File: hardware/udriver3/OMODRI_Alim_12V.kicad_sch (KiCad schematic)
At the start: 21 parts, among them U15 MP4572GQB, U9 TPSM560R6H

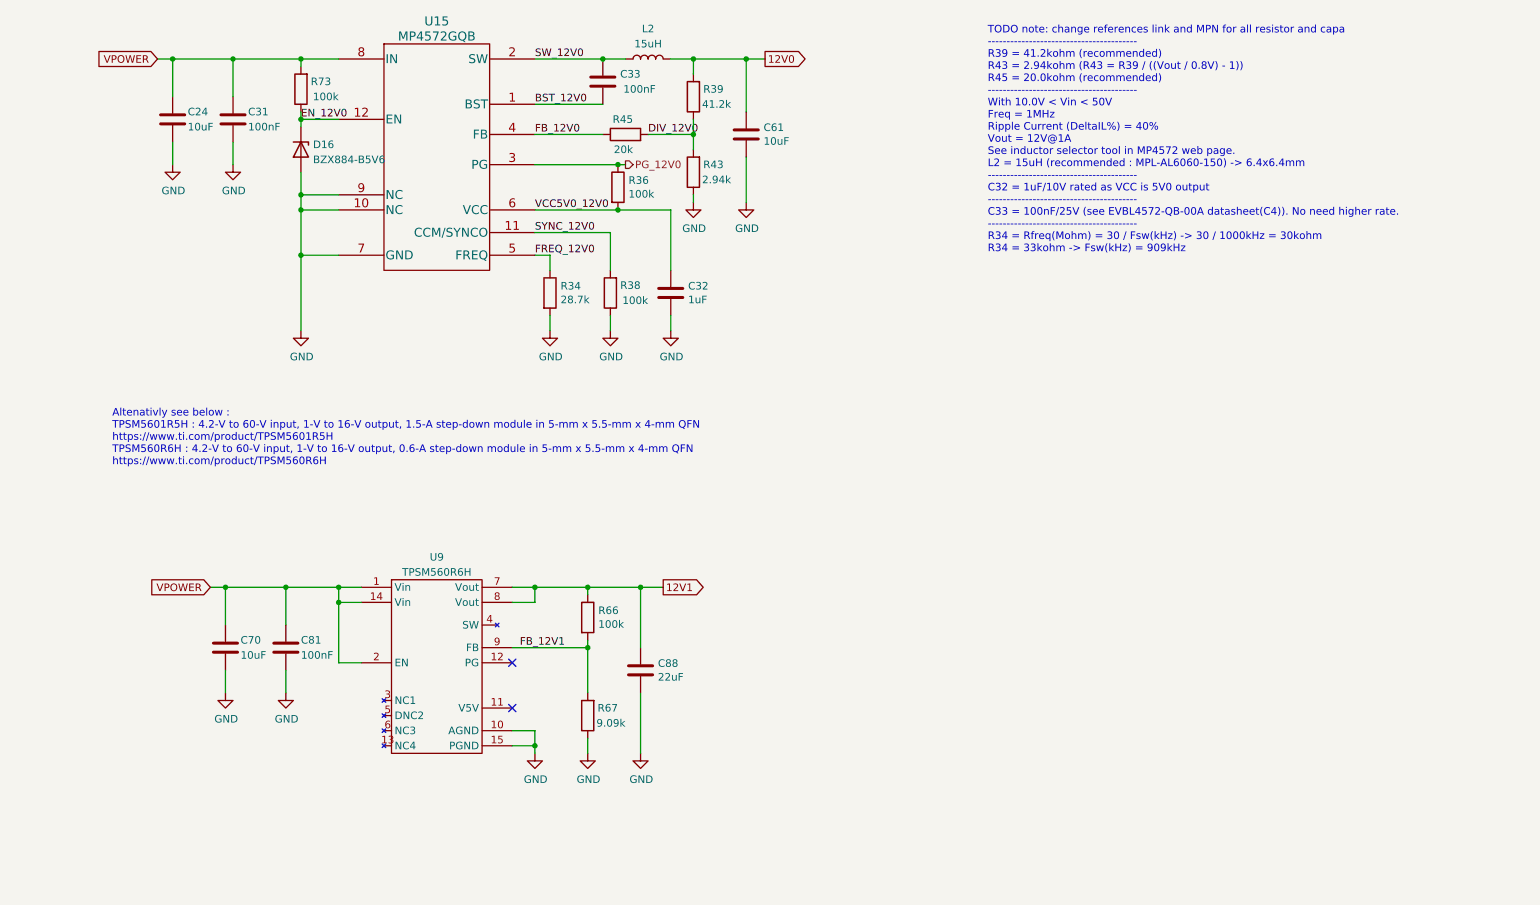
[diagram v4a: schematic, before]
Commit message: ORouting in progress. REF 3V0 missing.
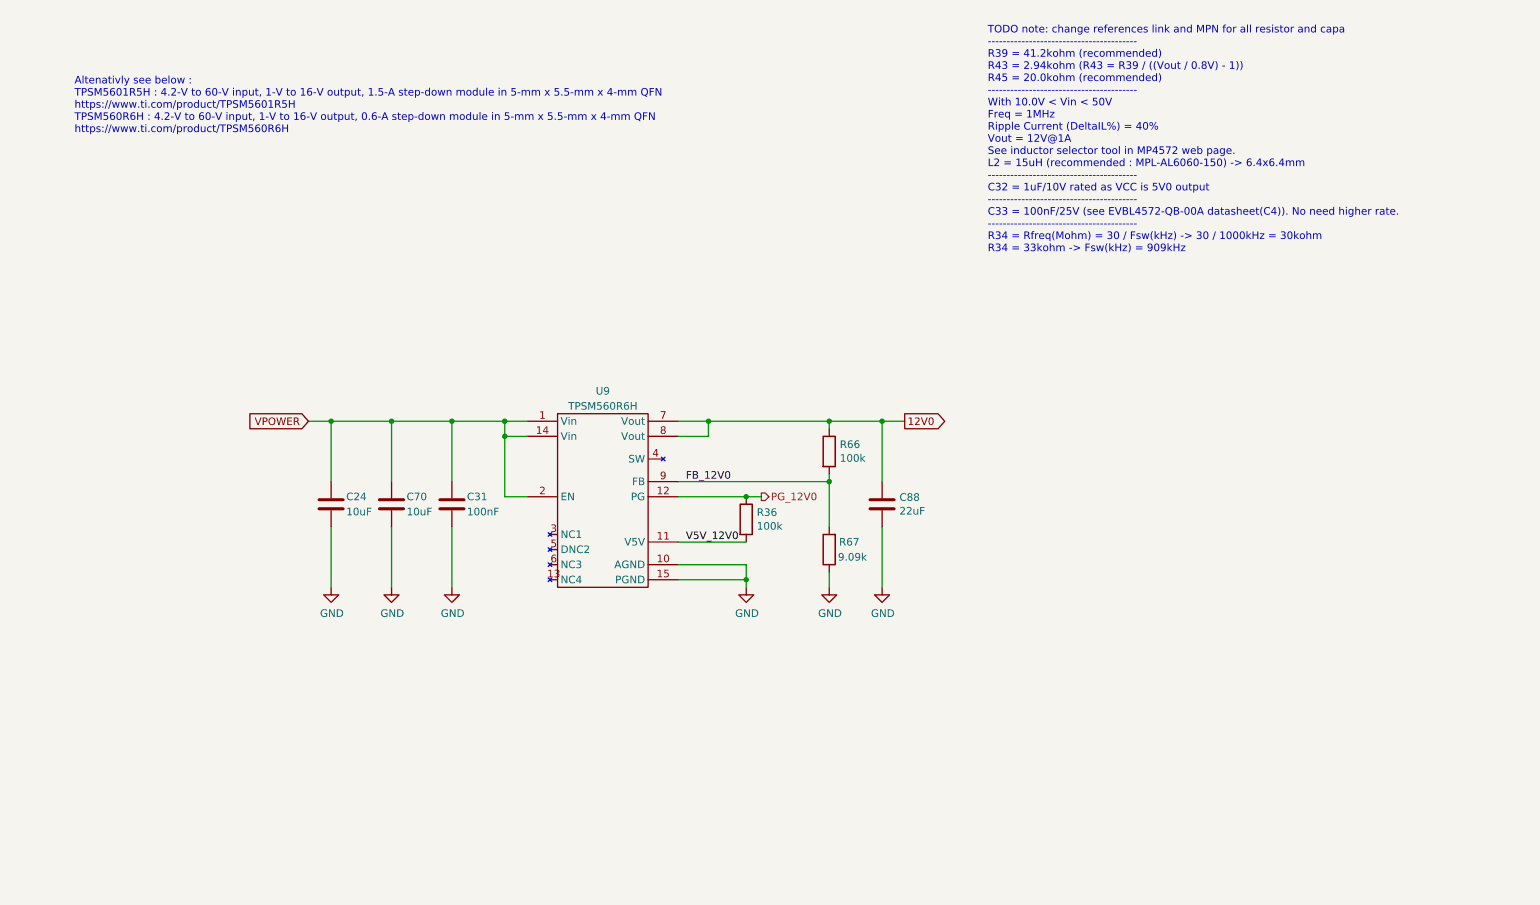
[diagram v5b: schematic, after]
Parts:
- removed C31: 100nF, Capacitor_SMD:C_0603_1608Metric, symbol Device:C
- removed C32: 1uF, Capacitor_SMD:C_0201_0603Metric, symbol Device:C
- removed C33: 100nF, Capacitor_SMD:C_0201_0603Metric, symbol Device:C
- removed C61: 10uF, Capacitor_SMD:C_0603_1608Metric, symbol Device:C
- removed D16: BZX884-B5V6, udriver3:DFN1006-2, symbol Device:D_Zener
- removed L2: 15uH, Inductor_SMD:L_Wuerth_MAPI-4020, symbol Device:L
- removed R34: 28.7k, Resistor_SMD:R_0201_0603Metric, symbol Device:R
- removed R38: 100k, Resistor_SMD:R_0201_0603Metric, symbol Device:R
- removed R39: 41.2k, Resistor_SMD:R_0201_0603Metric, symbol Device:R
- removed R43: 2.94k, Resistor_SMD:R_0201_0603Metric, symbol Device:R
- removed R45: 20k, Resistor_SMD:R_0201_0603Metric, symbol Device:R
- removed R73: 100k, Resistor_SMD:R_0402_1005Metric, symbol Device:R
- removed U15: MP4572GQB, udriver3:QFN-12_2.5x3mm_P0.5mm_MPS, symbol omodri_lib:MP4572GQB
- renumbered C81 to C31
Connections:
- net 12V1 is gone; now on net 12V0: C88.1, R66.1, U9.7 (Vout), U9.8 (Vout)
- net FB_12V1 is gone; now on net FB_12V0: R66.2, R67.2, U9.9 (FB)
- net VCC5V0_12V0 is gone; now on net V5V_12V0: R36.2
- net PG_12V0: now also U9.12 (PG)
- net V5V_12V0: now reaches U9.11 (V5V)
- no-connect marks 2 -> 0
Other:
- moved on the sheet: C31, C70, C88, R36, R66, R67, U9

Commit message: PCB fully routed. Some optimizations need to be done + revue of the schematics.
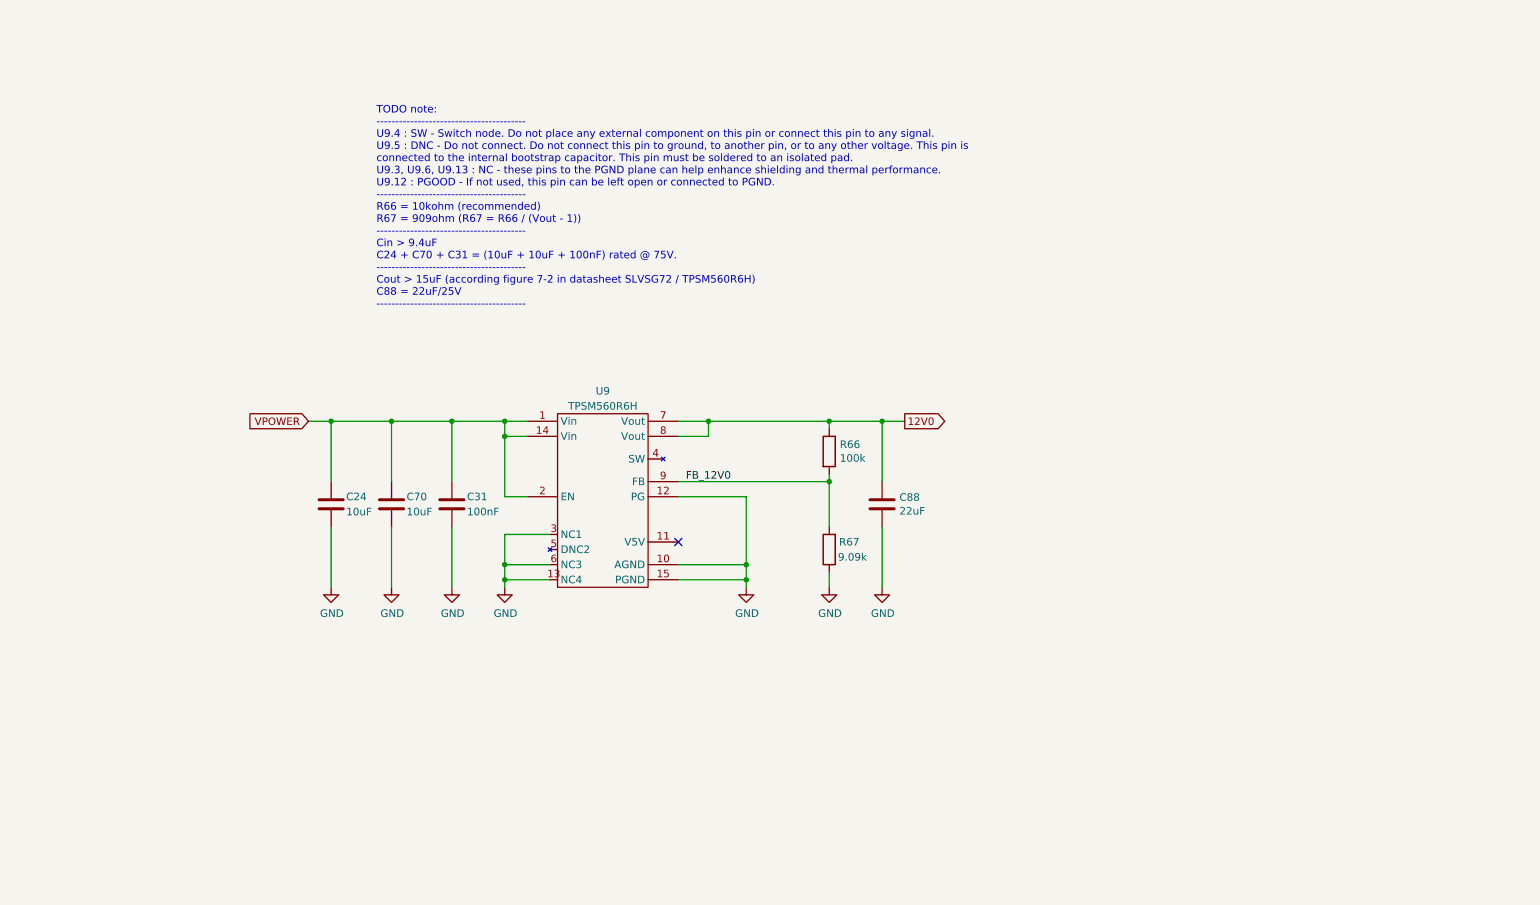
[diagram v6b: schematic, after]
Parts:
- removed R36: 100k, Resistor_SMD:R_0201_0603Metric, symbol Device:R
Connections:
- net PG_12V0 is gone; now on net GND: U9.12 (PG)
- net GND: now also U9.13 (NC4), U9.3 (NC1), U9.6 (NC3)
- net V5V_12V0: no longer names the net of U9.11 (V5V)
- no-connect marks 0 -> 1
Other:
- note added: "TODO note: ---------------------------------------- U9.4 : SW - Switch node. Do not place any external component on this pin or connect this pin to any signal. U9.5 : DNC - Do not connect. Do not connect this pin to ground, to another pin, or to any other voltage. This pin is connected to the internal bootstrap capacitor. This pin must be soldered to an isolated pad. U9.3, U9.6, U9.13 : NC - thes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"
- note removed: "Altenativly see below : TPSM5601R5H : 4.2-V to 60-V input, 1-V to 16-V output, 1.5-A step-down module in 5-mm x 5.5-mm x 4-mm QFN https://www.ti.com/product/TPSM5601R5H TPSM560R6H : 4.2-V to 60-V input, 1-V to 16-V output, 0.6-A step-down module in 5-mm x 5.5-mm x 4-mm QFN https://www.ti.com/product/TPSM560R6H"
- note removed: "TODO note: change references link and MPN for all resistor and capa ---------------------------------------- R39 = 41.2kohm (recommended) R43 = 2.94kohm (R43 = R39 / ((Vout / 0.8V) - 1)) R45 = 20.0kohm (recommended) ---------------------------------------- With 10.0V < Vin < 50V Freq = 1MHz Ripple Current (DeltaIL%) = 40% Vout = 12V@1A See inductor selector tool in MP4572 web page. L2 = 15uH (rec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"
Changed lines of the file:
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@@
   (junction (at 120.65 86.36) (diameter 0) (color 0 0 0 0)
   )
+  (junction (at 120.65 113.03) (diameter 0) (color 0 0 0 0)
+  )
   (junction (at 111.76 86.36) (diameter 0) (color 0 0 0 0)
   )
   (junction (at 101.6 86.36) (diameter 0) (color 0 0 0 0)
   )
+  (junction (at 120.65 110.49) (diameter 0) (color 0 0 0 0)
+  )
   (junction (at 91.44 86.36) (diameter 0) (color 0 0 0 0)
   )
@@
   (junction (at 175.26 86.36) (diameter 0) (color 0 0 0 0)
   )
-  (junction (at 161.29 99.06) (diameter 0) (color 0 0 0 0)
-  )
   (junction (at 161.29 113.03) (diameter 0) (color 0 0 0 0)
   )
+  (junction (at 161.29 110.49) (diameter 0) (color 0 0 0 0)
+  )
+  (no_connect (at 149.86 106.68))
   (wire (pts (xy 184.15 104.14) (xy 184.15 114.3))
     (stroke (width 0) (type default) (color 0 0 0 0))
@@
     (stroke (width 0) (type default) (color 0 0 0 0))
   )
+  (wire (pts (xy 149.86 99.06) (xy 161.29 99.06))
+    (stroke (width 0) (type default) (color 0 0 0 0))
+  )
   (wire (pts (xy 184.15 86.36) (xy 184.15 96.52))
     (stroke (width 0) (type default) (color 0 0 0 0))
   )
+  (wire (pts (xy 161.29 99.06) (xy 161.29 110.49))
+    (stroke (width 0) (type default) (color 0 0 0 0))
+  )
   (wire (pts (xy 175.26 96.52) (xy 175.26 104.14))
     (stroke (width 0) (type default) (color 0 0 0 0))
@@
     (stroke (width 0) (type default) (color 0 0 0 0))
   )
-  (wire (pts (xy 149.86 106.68) (xy 161.29 106.68))
+  (wire (pts (xy 120.65 105.41) (xy 128.27 105.41))
     (stroke (width 0) (type default) (color 0 0 0 0))
   )
@@
     (stroke (width 0) (type default) (color 0 0 0 0))
   )
-  (wire (pts (xy 149.86 99.06) (xy 161.29 99.06))
-    (stroke (width 0) (type default) (color 0 0 0 0))
-  )
   (wire (pts (xy 154.94 86.36) (xy 175.26 86.36))
     (stroke (width 0) (type default) (color 0 0 0 0))
@@
     (stroke (width 0) (type default) (color 0 0 0 0))
   )
+  (wire (pts (xy 120.65 110.49) (xy 120.65 113.03))
+    (stroke (width 0) (type default) (color 0 0 0 0))
+  )
   (wire (pts (xy 101.6 86.36) (xy 101.6 96.52))
     (stroke (width 0) (type default) (color 0 0 0 0))
@@
     (stroke (width 0) (type default) (color 0 0 0 0))
   )
+  (wire (pts (xy 120.65 113.03) (xy 120.65 114.3))
+    (stroke (width 0) (type default) (color 0 0 0 0))
+  )
   (wire (pts (xy 120.65 86.36) (xy 124.46 86.36))
     (stroke (width 0) (type default) (color 0 0 0 0))
   )
+  (wire (pts (xy 120.65 110.49) (xy 128.27 110.49))
+    (stroke (width 0) (type default) (color 0 0 0 0))
+  )
   (wire (pts (xy 175.26 111.76) (xy 175.26 114.3))
     (stroke (width 0) (type default) (color 0 0 0 0))
   )
-  (wire (pts (xy 161.29 99.06) (xy 163.83 99.06))
-    (stroke (width 0) (type default) (color 0 0 0 0))
-  )
   (wire (pts (xy 120.65 99.06) (xy 120.65 88.9))
     (stroke (width 0) (type default) (color 0 0 0 0))
@@
     (stroke (width 0) (type default) (color 0 0 0 0))
   )
-  (text "TODO note: change references link and MPN for all resistor and capa\n----------------------------------------\nR39 = 41.2kohm (recommended)\nR43 = 2.94kohm (R43 = R39 / ((Vout / 0.8V) - 1))\nR45 = 20.0kohm (recommended)\n----------------------------------------\nWith 10.0V < Vin < 50V\nFreq = 1MHz\nRipple Current (DeltaIL%) = 40%\nVout = 12V@1A\nSee inductor selector tool in MP4572 web page.\nL2 = 15uH (recommended : MPL-AL6060-150) -> 6.4x6.4mm\n----------------------------------------\nC32 = 1uF/10V rated as VCC is 5V0 output\n----------------------------------------\nC33 = 100nF/25V (see EVBL4572-QB-00A datasheet(C4)). No need higher rate.\n----------------------------------------\nR34 = Rfreq(Mohm) = 30 / Fsw(kHz) -> 30 / 1000kHz = 30kohm\nR34 = 33kohm -> Fsw(kHz) = 909kHz\n\n\n"
-    (at 201.93 62.23 0)
-    (effects (font (size 1.27 1.27)) (justify left bottom))
-  )
-  (text "Altenativly see below :\nTPSM5601R5H : 4.2-V to 60-V input, 1-V to 16-V output, 1.5-A step-down module in 5-mm x 5.5-mm x 4-mm QFN\nhttps://www.ti.com/product/TPSM5601R5H\nTPSM560R6H : 4.2-V to 60-V input, 1-V to 16-V output, 0.6-A step-down module in 5-mm x 5.5-mm x 4-mm QFN\nhttps://www.ti.com/product/TPSM560R6H"
-    (at 48.26 38.1 0)
-    (effects (font (size 1.27 1.27)) (justify left bottom))
-  )
-  (label "V5V_12V0" (at 151.13 106.68 0)
+  (wire (pts (xy 120.65 105.41) (xy 120.65 110.49))
+    (stroke (width 0) (type default) (color 0 0 0 0))
+  )
+  (wire (pts (xy 120.65 113.03) (xy 128.27 113.03))
+    (stroke (width 0) (type default) (color 0 0 0 0))
+  )
+  (text "TODO note:\n----------------------------------------\nU9.4 : SW - Switch node. Do not place any external component on this pin or connect this pin to any signal.\nU9.5 : DNC - Do not connect. Do not connect this pin to ground, to another pin, or to any other voltage. This pin is\nconnected to the internal bootstrap capacitor. This pin must be soldered to an isolated pad.\nU9.3, U9.6, U9.13 : NC - these pins to the PGND plane can help enhance shielding and thermal performance.\nU9.12 : PGOOD - If not used, this pin can be left open or connected to PGND.\n----------------------------------------\nR66 = 10kohm (recommended)\nR67 = 909ohm (R67 = R66 / (Vout - 1))\n----------------------------------------\nCin > 9.4uF\nC24 + C70 + C31 = (10uF + 10uF + 100nF) rated @ 75V.\n----------------------------------------\nCout > 15uF (according figure 7-2 in datasheet SLVSG72 / TPSM560R6H)\nC88 = 22uF/25V\n----------------------------------------\n\n\n\n"
+    (at 99.06 73.66 0)
     (effects (font (size 1.27 1.27)) (justify left bottom))
   )
@@
       (effects (font (size 1.27 1.27)) (justify left) hide)
     )
-  )
-  (hierarchical_label "PG_12V0" (shape output) (at 163.83 99.06 0)
-    (effects (font (size 1.27 1.27)) (justify left))
   )
   (symbol (lib_id "power:GND") (at 184.15 114.3 0) (unit 1)
@@
     (pin "2")
   )
+  (symbol (lib_id "power:GND") (at 120.65 114.3 0) (unit 1)
+    (in_bom yes) (on_board yes)
+    (property "Reference" "#PWR0119" (id 0) (at 120.65 120.65 0)
+      (effects (font (size 1.27 1.27)) hide)
+    )
+    (property "Value" "GND" (id 1) (at 120.777 118.6942 0))
+    (property "Footprint" "" (id 2) (at 120.65 114.3 0)
+      (effects (font (size 1.27 1.27)) hide)
+    )
+    (property "Datasheet" "" (id 3) (at 120.65 114.3 0)
+      (effects (font (size 1.27 1.27)) hide)
+    )
+    (pin "1")
+  )
   (symbol (lib_id "power:GND") (at 175.26 114.3 0) (unit 1)
     (in_bom yes) (on_board yes)
@@
     (pin "1")
   )
-  (symbol (lib_id "Device:R") (at 161.29 102.87 0) (unit 1)
-    (in_bom yes) (on_board yes)
-    (property "Reference" "R36" (id 0) (at 163.068 101.7016 0)
-      (effects (font (size 1.27 1.27)) (justify left))
-    )
-    (property "Value" "100k" (id 1) (at 163.068 104.013 0)
-      (effects (font (size 1.27 1.27)) (justify left))
-    )
-    (property "Footprint" "Resistor_SMD:R_0201_0603Metric" (id 2) (at 159.512 102.87 90)
-      (effects (font (size 1.27 1.27)) hide)
-    )
-    (property "Datasheet" "~" (id 3) (at 161.29 102.87 0)
-      (effects (font (size 1.27 1.27)) hide)
-    )
-    (property "DigiKey" "P122655CT-ND" (id 4) (at 161.29 102.87 0)
-      (effects (font (size 1.27 1.27)) hide)
-    )
-    (property "Farnell" "2302389" (id 5) (at 161.29 102.87 0)
-      (effects (font (size 1.27 1.27)) hide)
-    )
-    (property "Mouser" "667-ERJ-1GNF1003C" (id 6) (at 161.29 102.87 0)
-      (effects (font (size 1.27 1.27)) hide)
-    )
-    (property "Part No" "ERJ-1GNF1003C" (id 7) (at 161.29 102.87 0)
-      (effects (font (size 1.27 1.27)) hide)
-    )
-    (property "RS" "179-7130" (id 8) (at 161.29 102.87 0)
-      (effects (font (size 1.27 1.27)) hide)
-    )
-    (pin "1")
-    (pin "2")
-  )
   (symbol (lib_id "power:GND") (at 161.29 114.3 0) (unit 1)
